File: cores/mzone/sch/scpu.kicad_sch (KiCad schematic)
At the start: 75 parts, among them X1 14.318MHZ

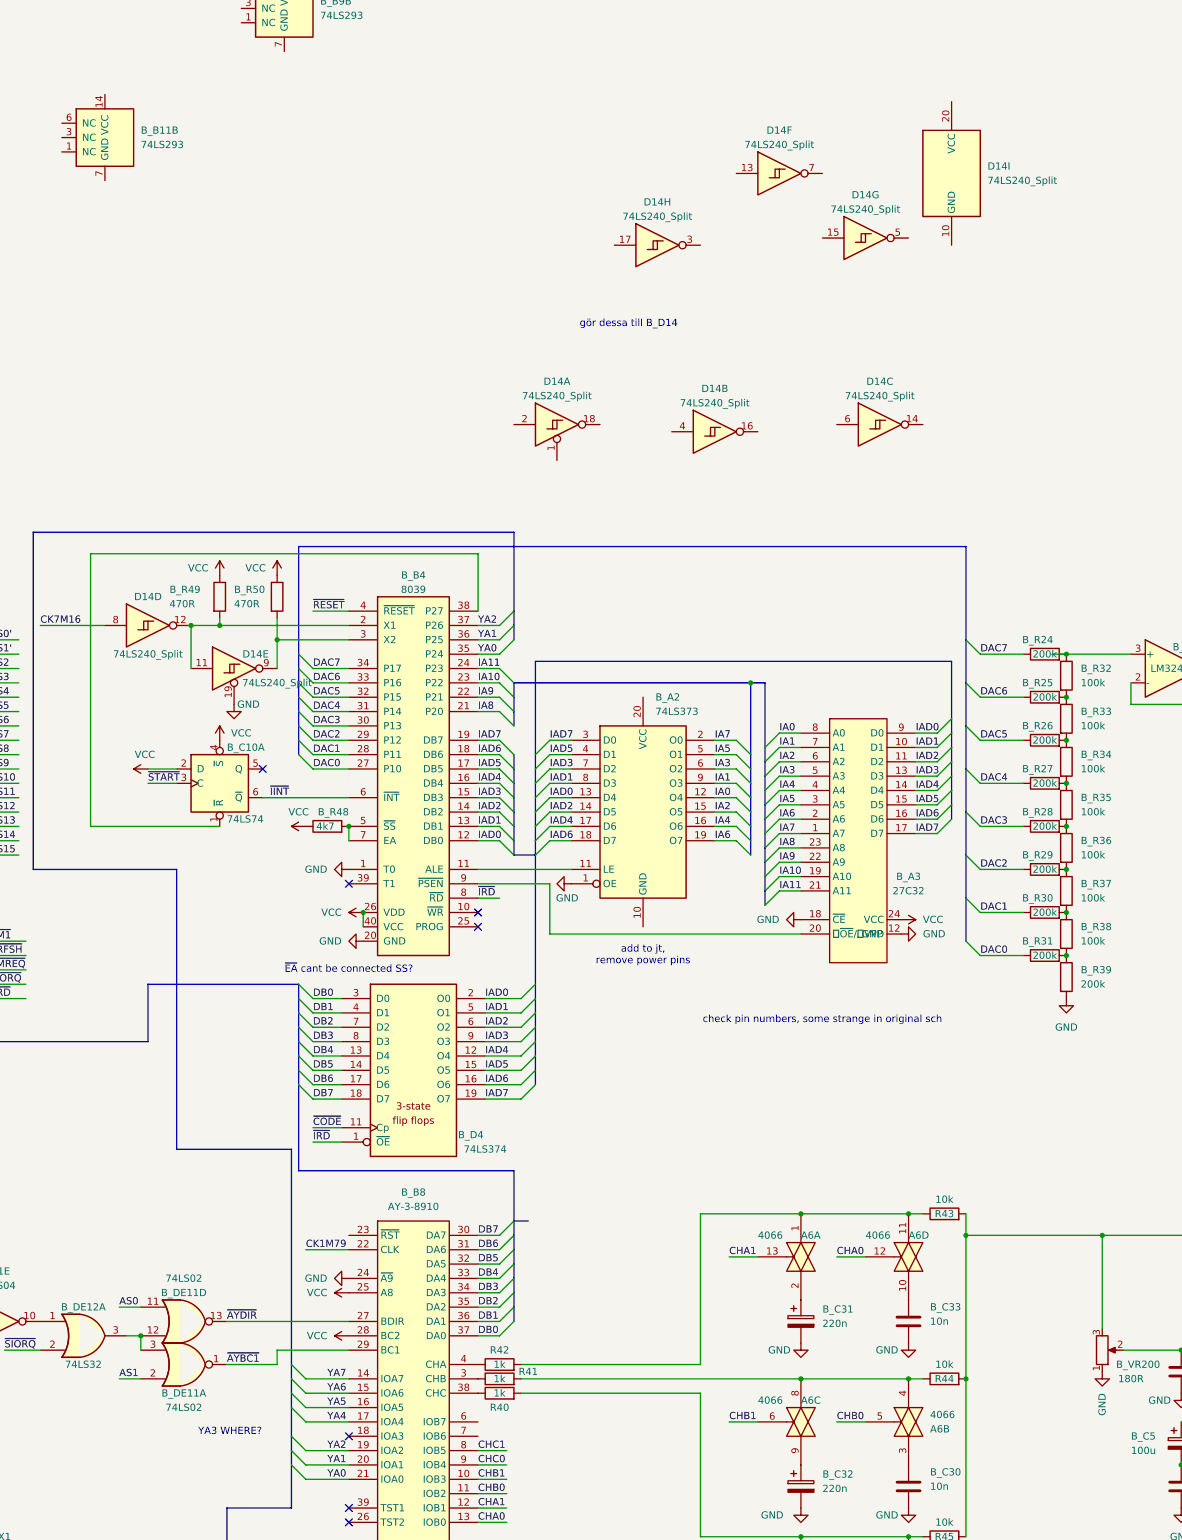
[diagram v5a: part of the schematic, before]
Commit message: mzone core
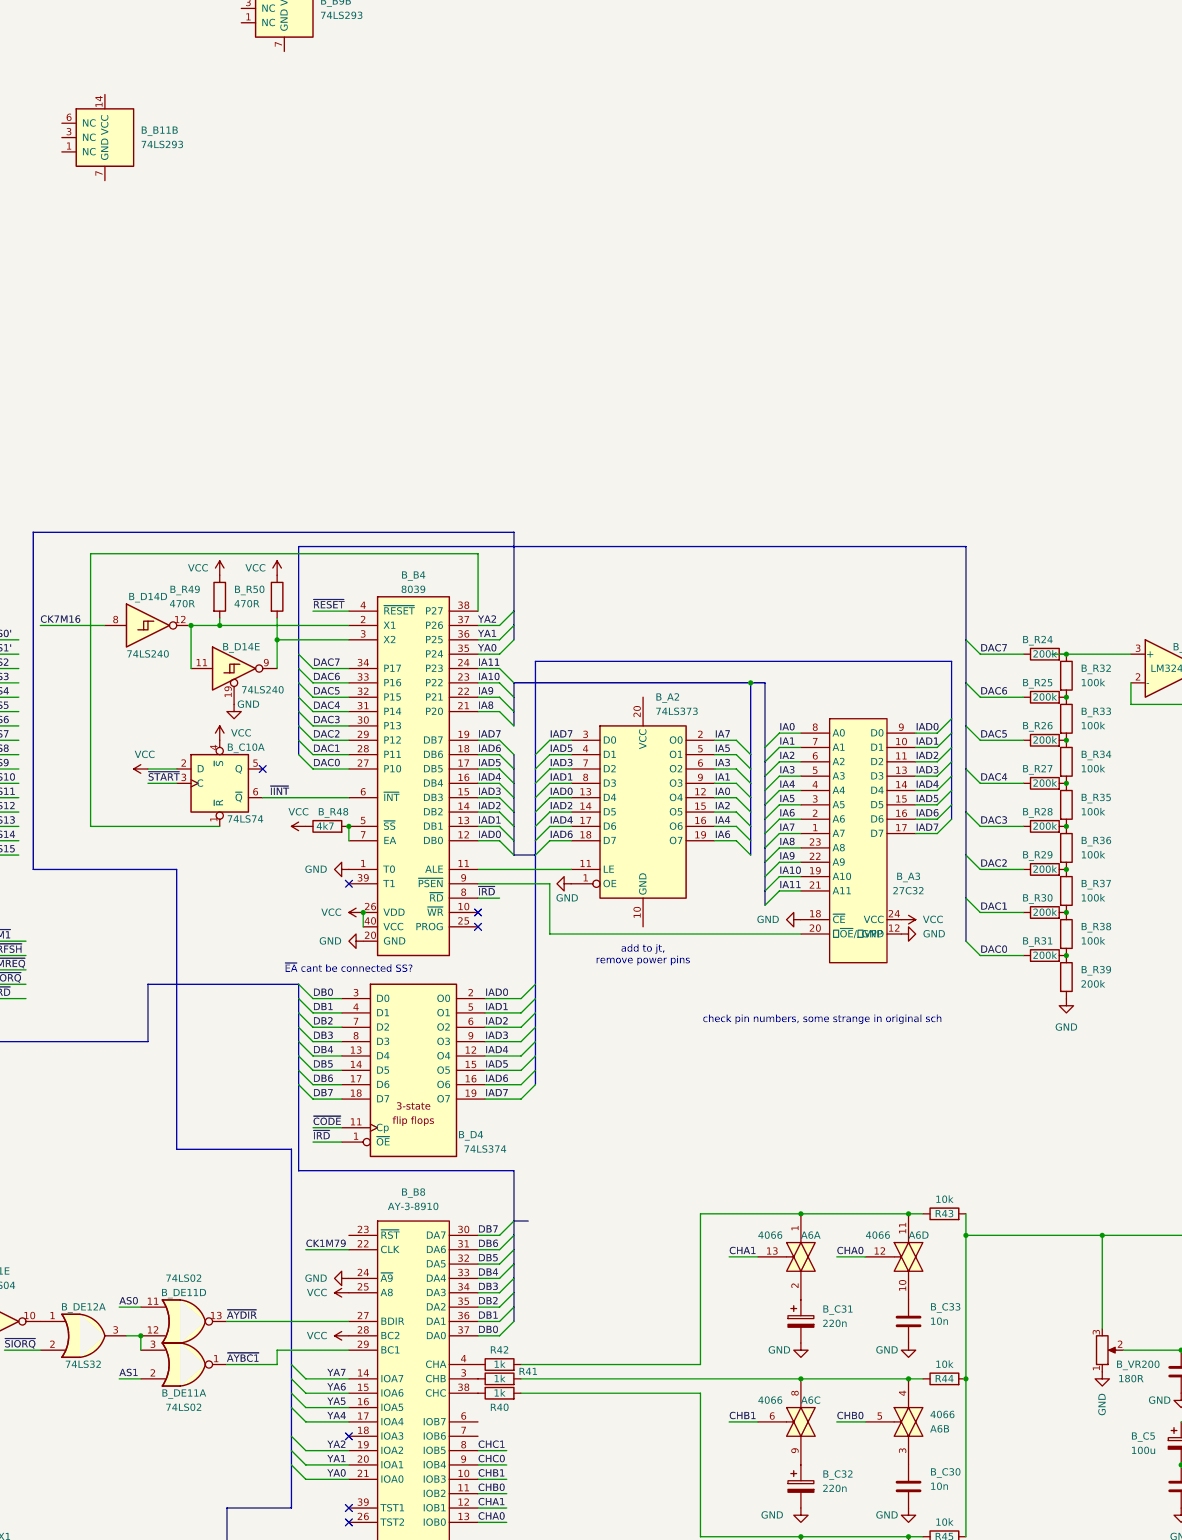
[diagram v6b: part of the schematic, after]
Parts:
- removed D14: 74LS240_Split, symbol 74xx:74LS240_Split
- added B_D14: 74LS240, symbol 74xx:74LS240_Split
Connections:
- net CK7M16: now also B_D14.8
- net GND: now also B_D14.19
- net at B_B4.2 (X1), B_R49.2: now also B_D14.11, B_D14.12
- net at B_B4.3 (X2), B_R50.2: now also B_D14.9
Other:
- note removed: "YA3 WHERE?"
- note removed: "gör dessa till B_D14"
